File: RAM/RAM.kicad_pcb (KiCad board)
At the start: 2 copper layers, 133 x 58.5 mm, 60 parts, among them J1 Conn_01x02_Pin, J2 Conn_01x01_Pin, J3 Conn_01x02_Pin, J4 Conn_01x01_Pin, J5 Conn_01x05_Pin, J6 Conn_01x03_Pin, J7 Conn_01x03_Pin, J8 Conn_01x03_Pin, J9 Conn_01x10_Pin, U2 CD74HCT258E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

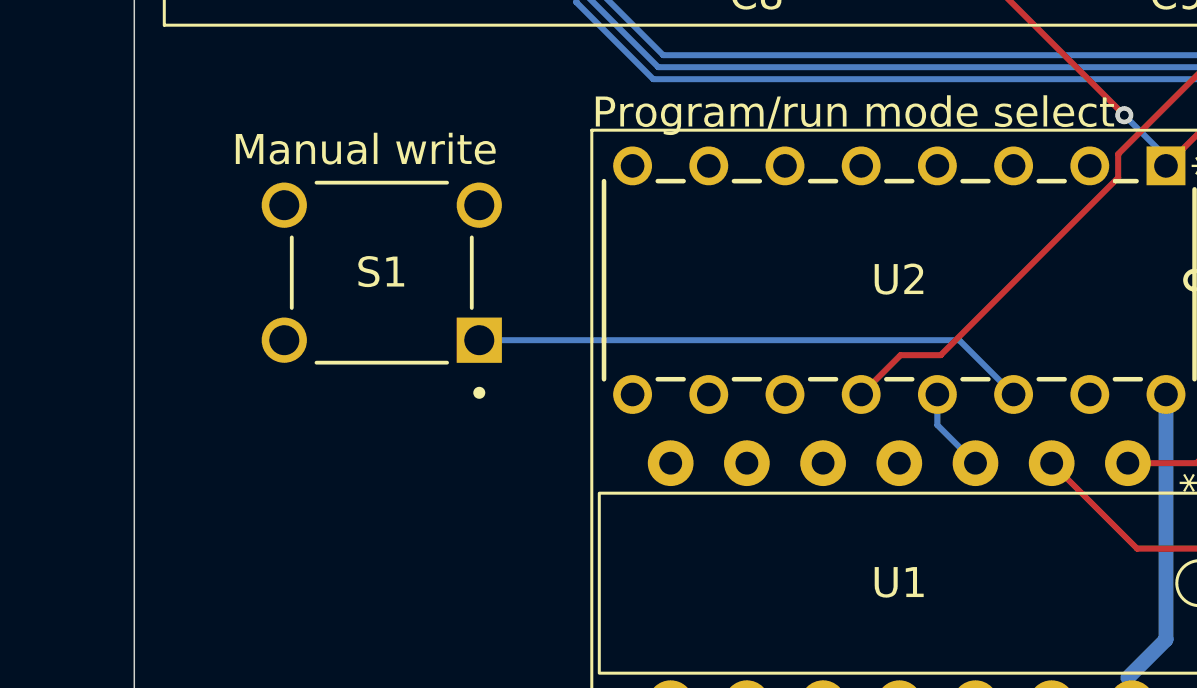
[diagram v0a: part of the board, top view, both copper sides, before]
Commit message: Added a pull up resistor to the programming button
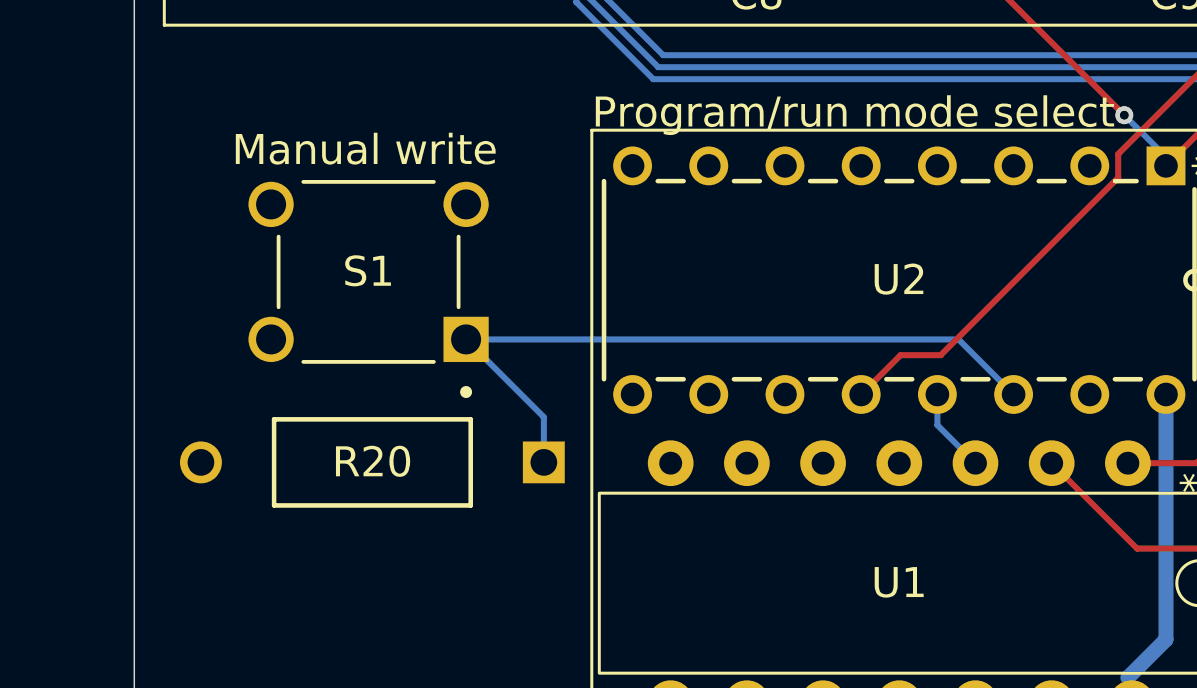
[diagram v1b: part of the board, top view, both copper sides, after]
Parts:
- added R20: 10k, _DownloadFootprints:CF_series_Resistors_THT, F.Cu at (136.7, 84.1)
- moved S1 0.44 mm to (130.8, 77.7)
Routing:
- net Net-(U2-4A): track 18.6 -> 24.2 mm

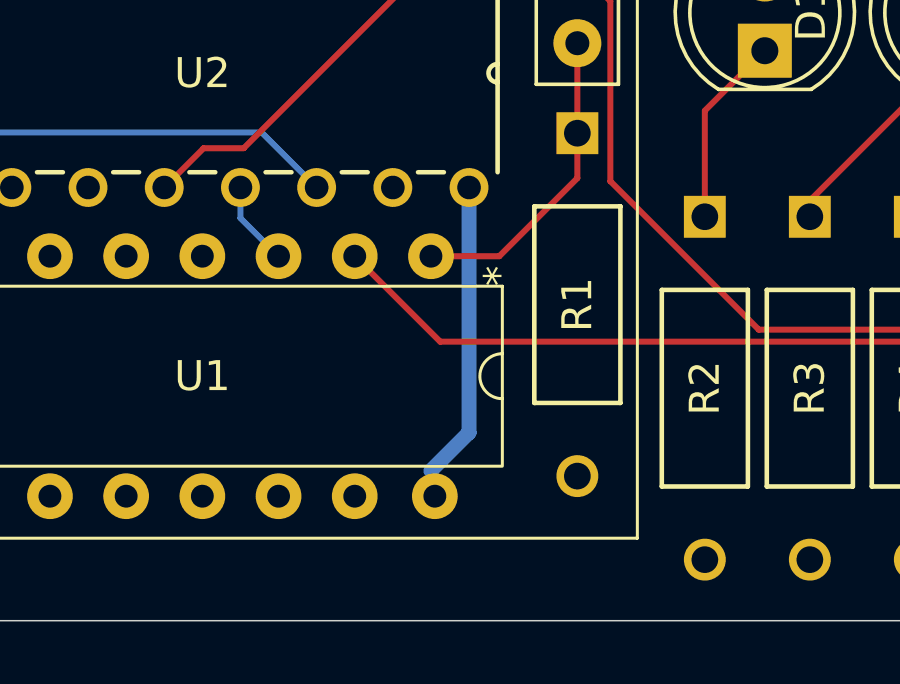
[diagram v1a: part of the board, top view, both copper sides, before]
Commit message: Fixed barely connected power wire
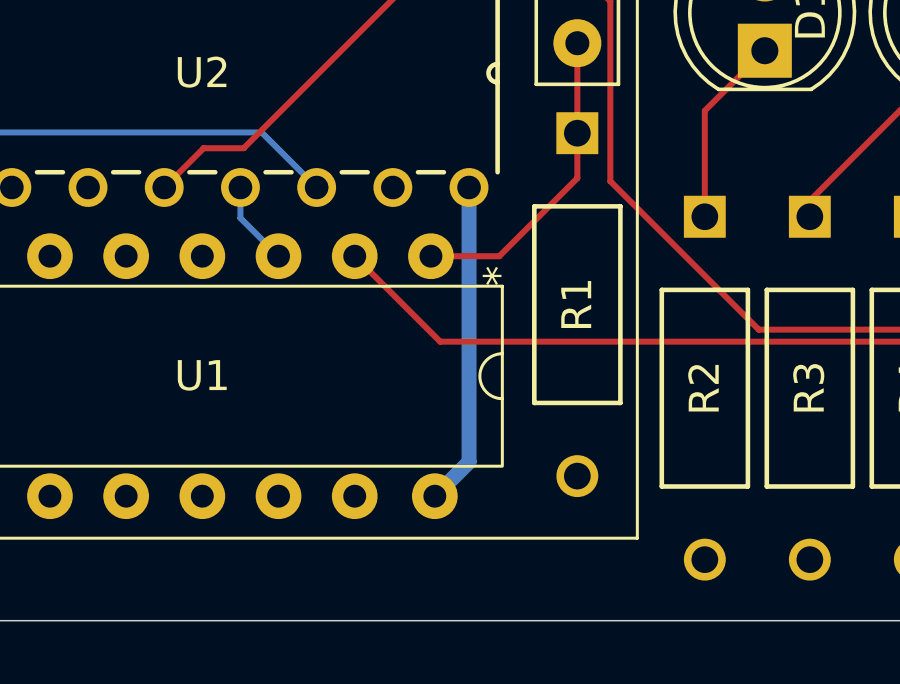
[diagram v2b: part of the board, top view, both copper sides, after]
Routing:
- net +5V: track 65.1 -> 65.9 mm
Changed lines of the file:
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@@
 	)
 	(segment
-		(start 204.38 59.38)
-		(end 204.38 57)
+		(start 157.39 90.96)
+		(end 156.25 92.1)
 		(width 0.5)
 		(layer "B.Cu")
@@
 	)
 	(segment
-		(start 157.39 89.98)
-		(end 156.12 91.25)
+		(start 204.38 59.38)
+		(end 204.38 57)
 		(width 0.5)
 		(layer "B.Cu")
@@
 	(segment
 		(start 157.39 81.81)
-		(end 157.39 89.98)
+		(end 157.39 90.96)
 		(width 0.5)
 		(layer "B.Cu")
